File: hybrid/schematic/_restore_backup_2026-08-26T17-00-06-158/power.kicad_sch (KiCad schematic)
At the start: 15 parts, among them J1 24V_In, U1 LM2596S-5, U2 AMS1117-3.3

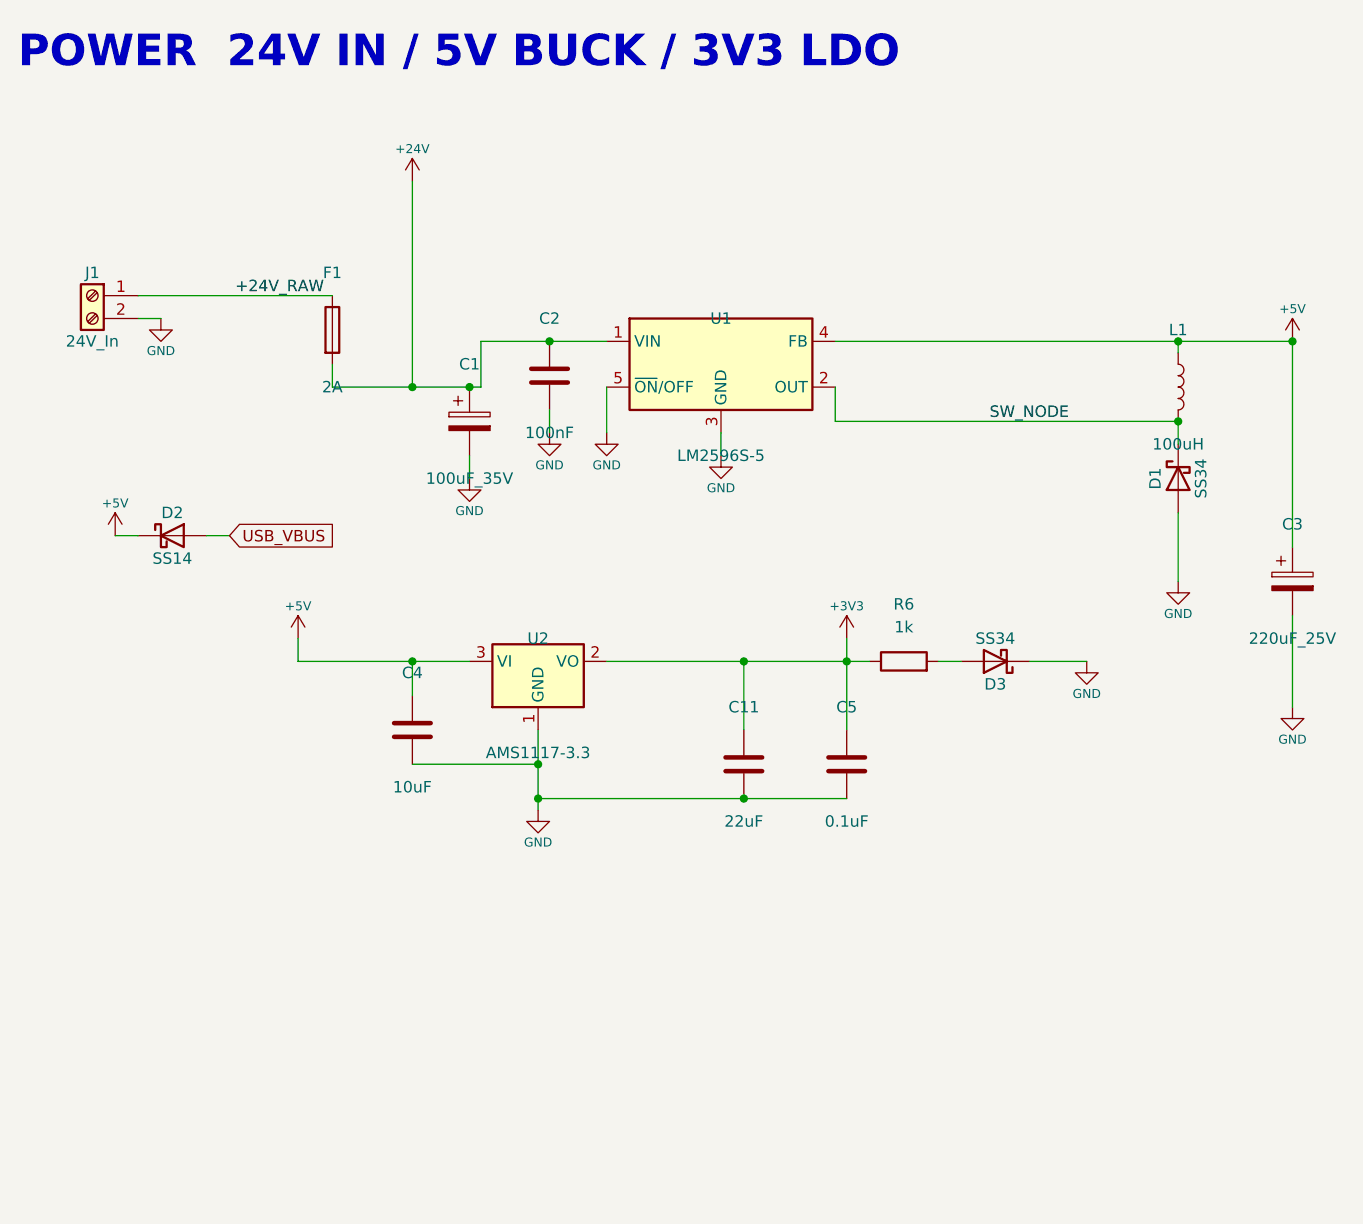
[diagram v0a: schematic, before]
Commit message: fullpcb filled out
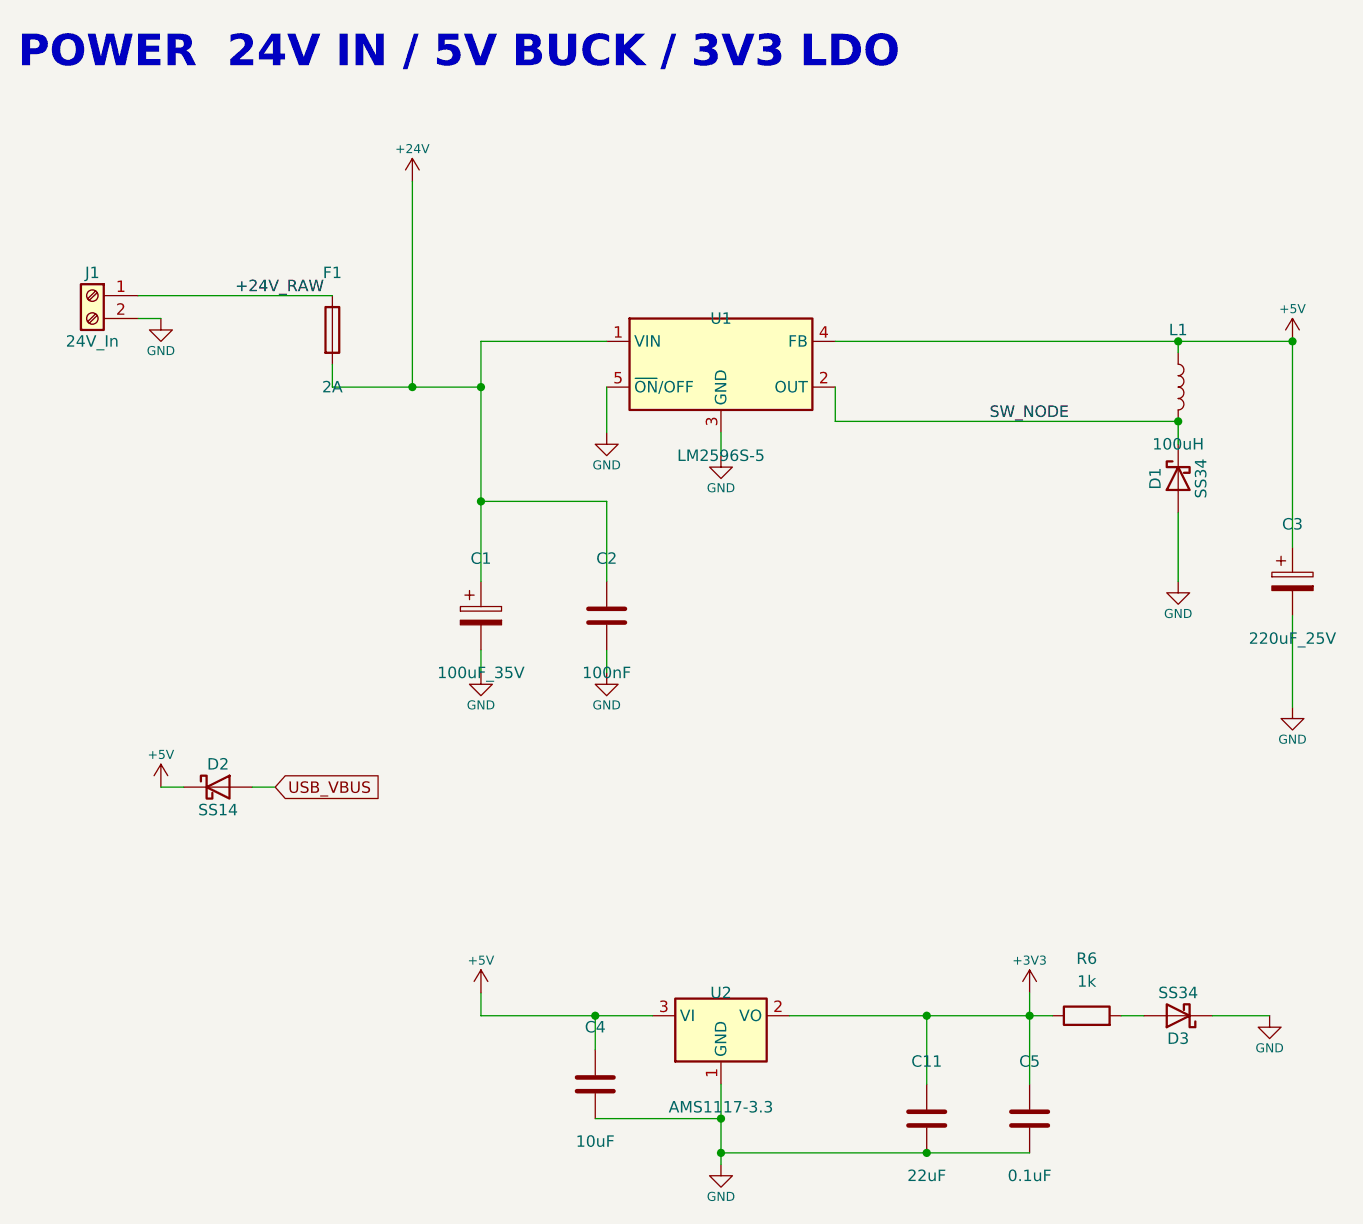
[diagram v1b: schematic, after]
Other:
- moved on the sheet: C1, C11, C2, C4, C5, D2, D3, R6, U2
